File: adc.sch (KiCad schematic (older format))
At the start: 89 parts, among them CN14 10nF, CN17 10nF, CN5 10nF, CN6 10nF, U35 MCP6004, U36 MCP6004, U46 MCP6004, U8 MCP6004

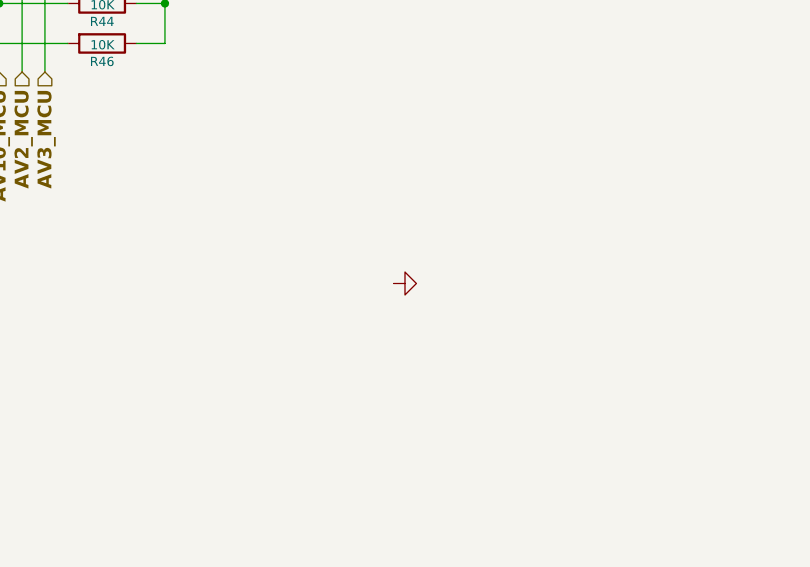
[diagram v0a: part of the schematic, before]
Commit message: Missing GND connection on CRNK-
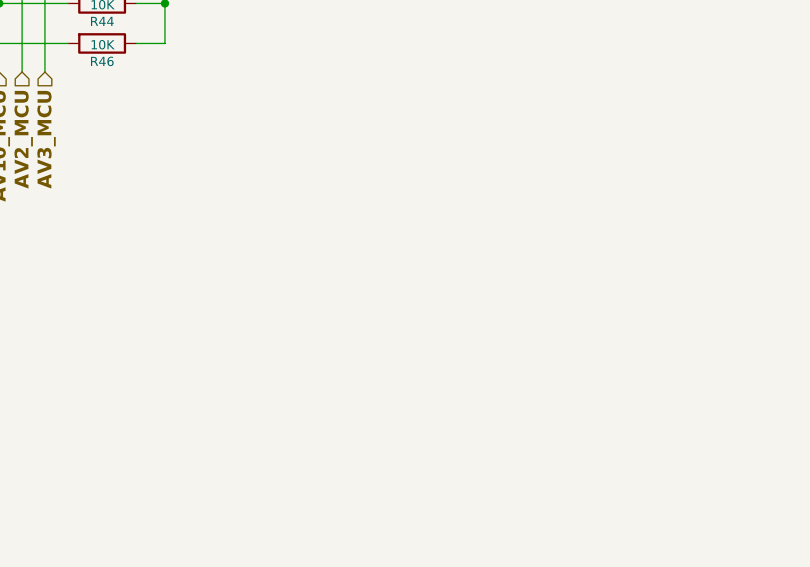
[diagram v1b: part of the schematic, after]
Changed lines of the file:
@@
 Text HLabel 8475 4800 2    60   Input ~ 12
 AGND
-$Comp
-L power:GND #PWR0139
-U 1 1 5D996BA6
-P 9475 6125
-F 0 "#PWR0139" H 9475 6125 30  0001 C CNN
-F 1 "GND" H 9475 6055 30  0001 C CNN
-F 2 "" H 9475 6125 60  0000 C CNN
-F 3 "" H 9475 6125 60  0000 C CNN
-	1    9475 6125
-	0    -1   -1   0
-$EndComp
 Wire Wire Line
 	8350 4550 8475 4550
